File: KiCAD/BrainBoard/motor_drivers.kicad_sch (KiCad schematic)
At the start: 4 parts, among them U2 DRV8231ADSG

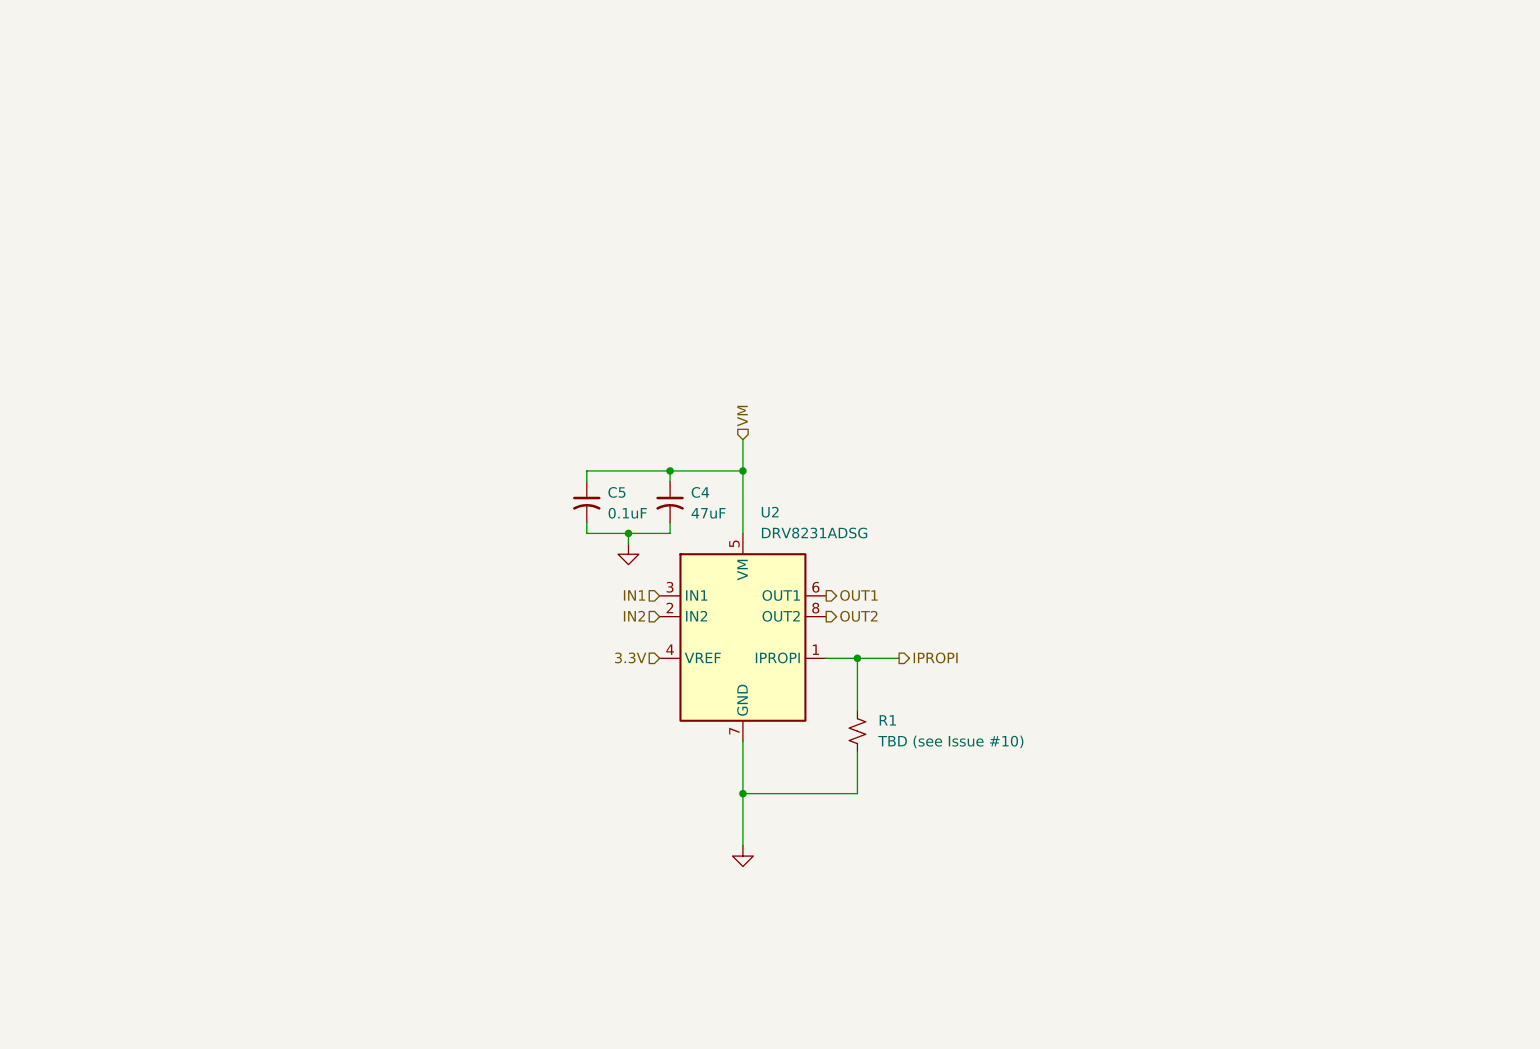
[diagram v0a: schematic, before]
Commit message: [feature] Finalize DRV8231DSGR motor drivers
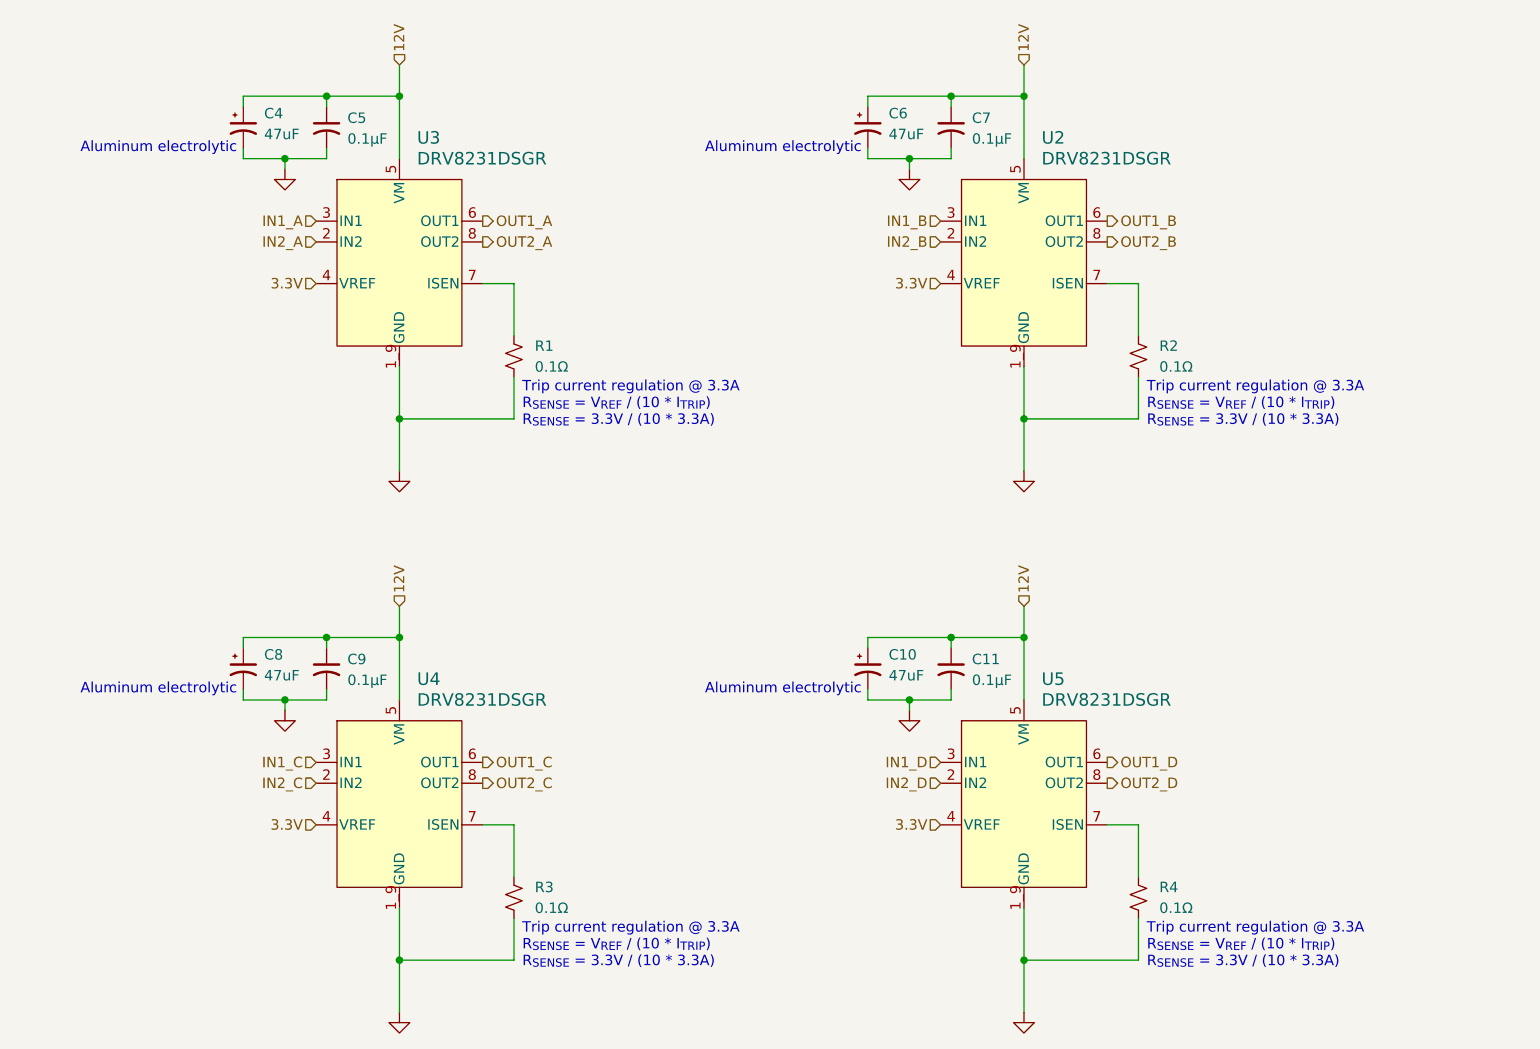
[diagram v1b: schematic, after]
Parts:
- removed C4: 47uF, symbol Device:C_Small_US
- removed U2: DRV8231ADSG, Package_SON:WSON-8-1EP_2x2mm_P0.5mm_EP0.9x1.6mm, symbol Driver_Motor:DRV8231ADSG
- added C10, C4, C6, C8: 47uF, symbol Device:C_Polarized_Small_US
- added C11, C7, C9: 0.1µF, symbol Device:C_Small_US
- added R2, R3, R4: 0.1Ω, symbol Device:R_Small_US
- added U2, U3, U4, U5: DRV8231DSGR, WSON8_DRV8231_TEX, symbol DRV8231DSGR:DRV8231DSGR
- C5: value 0.1uF -> 0.1µF
- R1: value TBD (see Issue #10) -> 0.1Ω
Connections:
- net 3.3V: now also U2.4 (VREF), U3.4 (VREF), U4.4 (VREF), U5.4 (VREF)
- net GND: now also C10.2, C11.2, C4.2, C6.2, C7.2, C8.2, C9.2, R2.2, R3.2, R4.2, U2.1_9 (GND), U3.1_9 (GND), U4.1_9 (GND), U5.1_9 (GND)
- net IPROPI: no longer names the net of R1.1
- net IPROPI: now also U3.7 (ISEN)
- net VM renamed 12V
- net 12V: now also C10.1, C11.1, C4.1, C6.1, C7.1, C8.1, C9.1, U2.5 (VM), U3.5 (VM), U4.5 (VM), U5.5 (VM)
- new net: R3.1, U4.7 (ISEN)
- new net: R2.1, U2.7 (ISEN)
- new net: R4.1, U5.7 (ISEN)
- new net IN1_A: U3.3 (IN1)
- new net IN1_B: U2.3 (IN1)
- new net IN1_C: U4.3 (IN1)
- new net IN1_D: U5.3 (IN1)
- new net IN2_A: U3.2 (IN2)
- new net IN2_B: U2.2 (IN2)
- new net IN2_C: U4.2 (IN2)
- new net IN2_D: U5.2 (IN2)
- new net OUT1_A: U3.6 (OUT1)
- new net OUT1_B: U2.6 (OUT1)
- new net OUT1_C: U4.6 (OUT1)
- new net OUT1_D: U5.6 (OUT1)
- new net OUT2_A: U3.8 (OUT2)
- new net OUT2_B: U2.8 (OUT2)
- new net OUT2_C: U4.8 (OUT2)
- new net OUT2_D: U5.8 (OUT2)
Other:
- note added: "Aluminum electrolytic"
- note added: "Trip current regulation @ 3.3A R_{SENSE} = V_{REF} / (10 * I_{TRIP}) R_{SENSE} = 3.3V / (10 * 3.3A)"
- moved on the sheet: C5, R1

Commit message: fix: Make DRC happy
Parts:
- U2, U3, U4, U5: footprint WSON8_DRV8231_TEX -> footprints:WSON8_DRV8231_TEX
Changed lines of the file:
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@@
 			)
 		)
-		(property "Footprint" "WSON8_DRV8231_TEX"
+		(property "Footprint" "footprints:WSON8_DRV8231_TEX"
 			(at 97.79 50.8 0)
 			(effects
@@
 			)
 		)
-		(property "Footprint" "WSON8_DRV8231_TEX"
+		(property "Footprint" "footprints:WSON8_DRV8231_TEX"
 			(at 173.99 50.8 0)
 			(effects
@@
 			)
 		)
-		(property "Footprint" "WSON8_DRV8231_TEX"
+		(property "Footprint" "footprints:WSON8_DRV8231_TEX"
 			(at 97.79 116.84 0)
 			(effects
@@
 			)
 		)
-		(property "Footprint" "WSON8_DRV8231_TEX"
+		(property "Footprint" "footprints:WSON8_DRV8231_TEX"
 			(at 173.99 116.84 0)
 			(effects

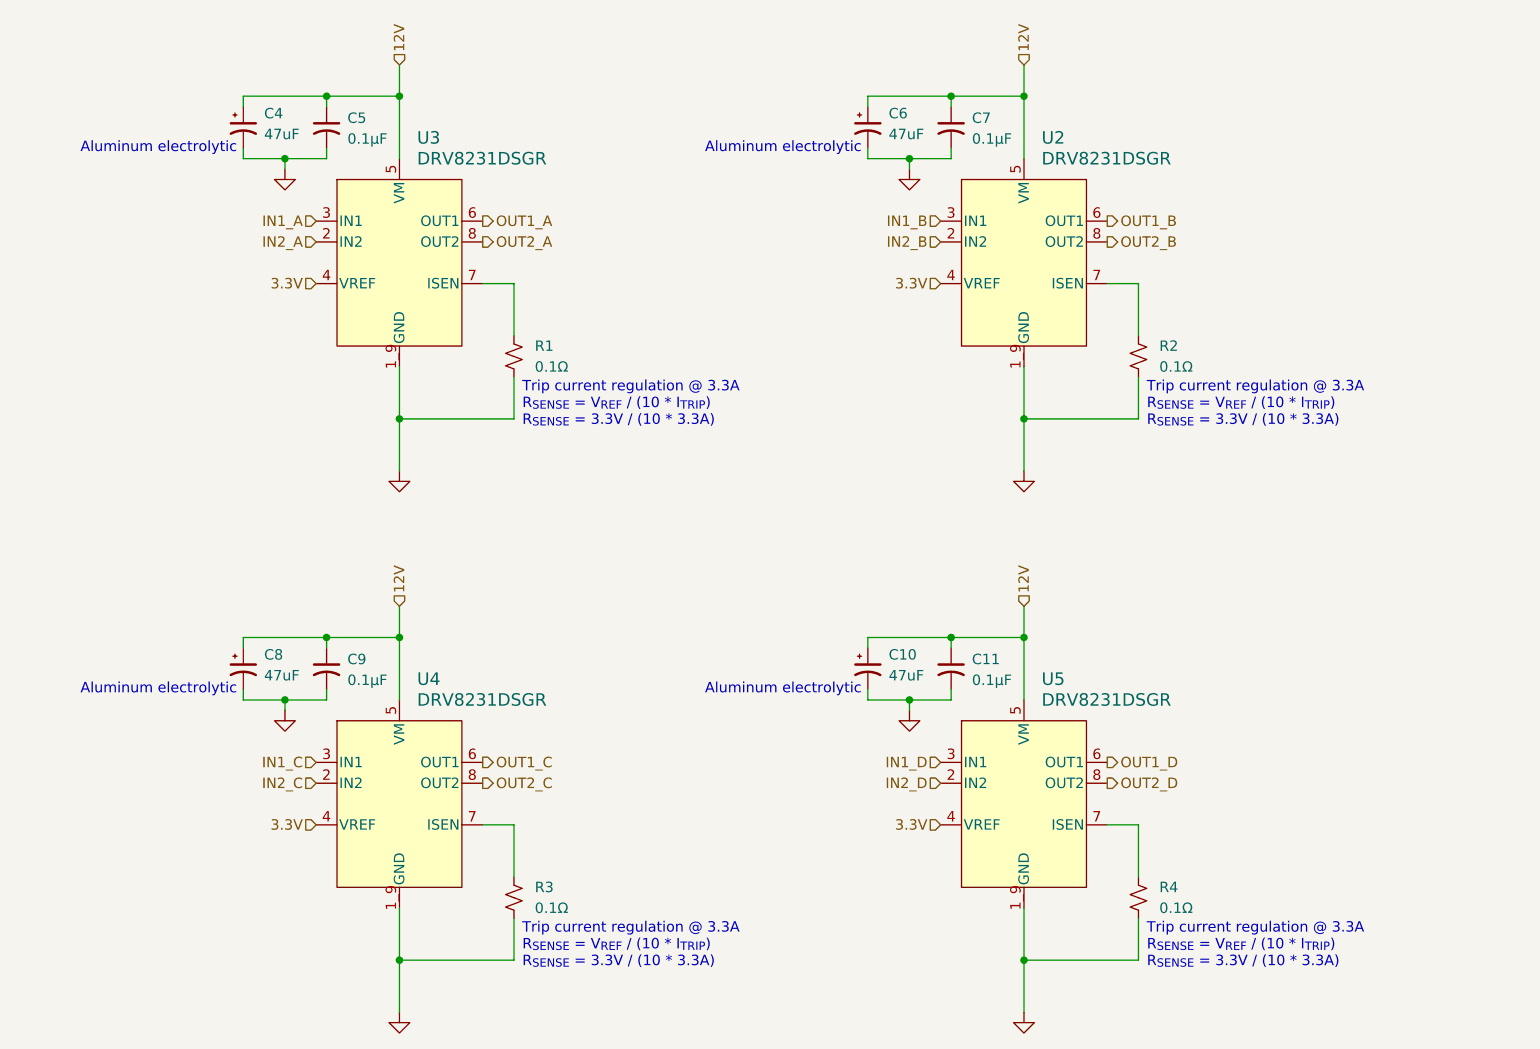
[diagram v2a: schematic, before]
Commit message: feat: battery input
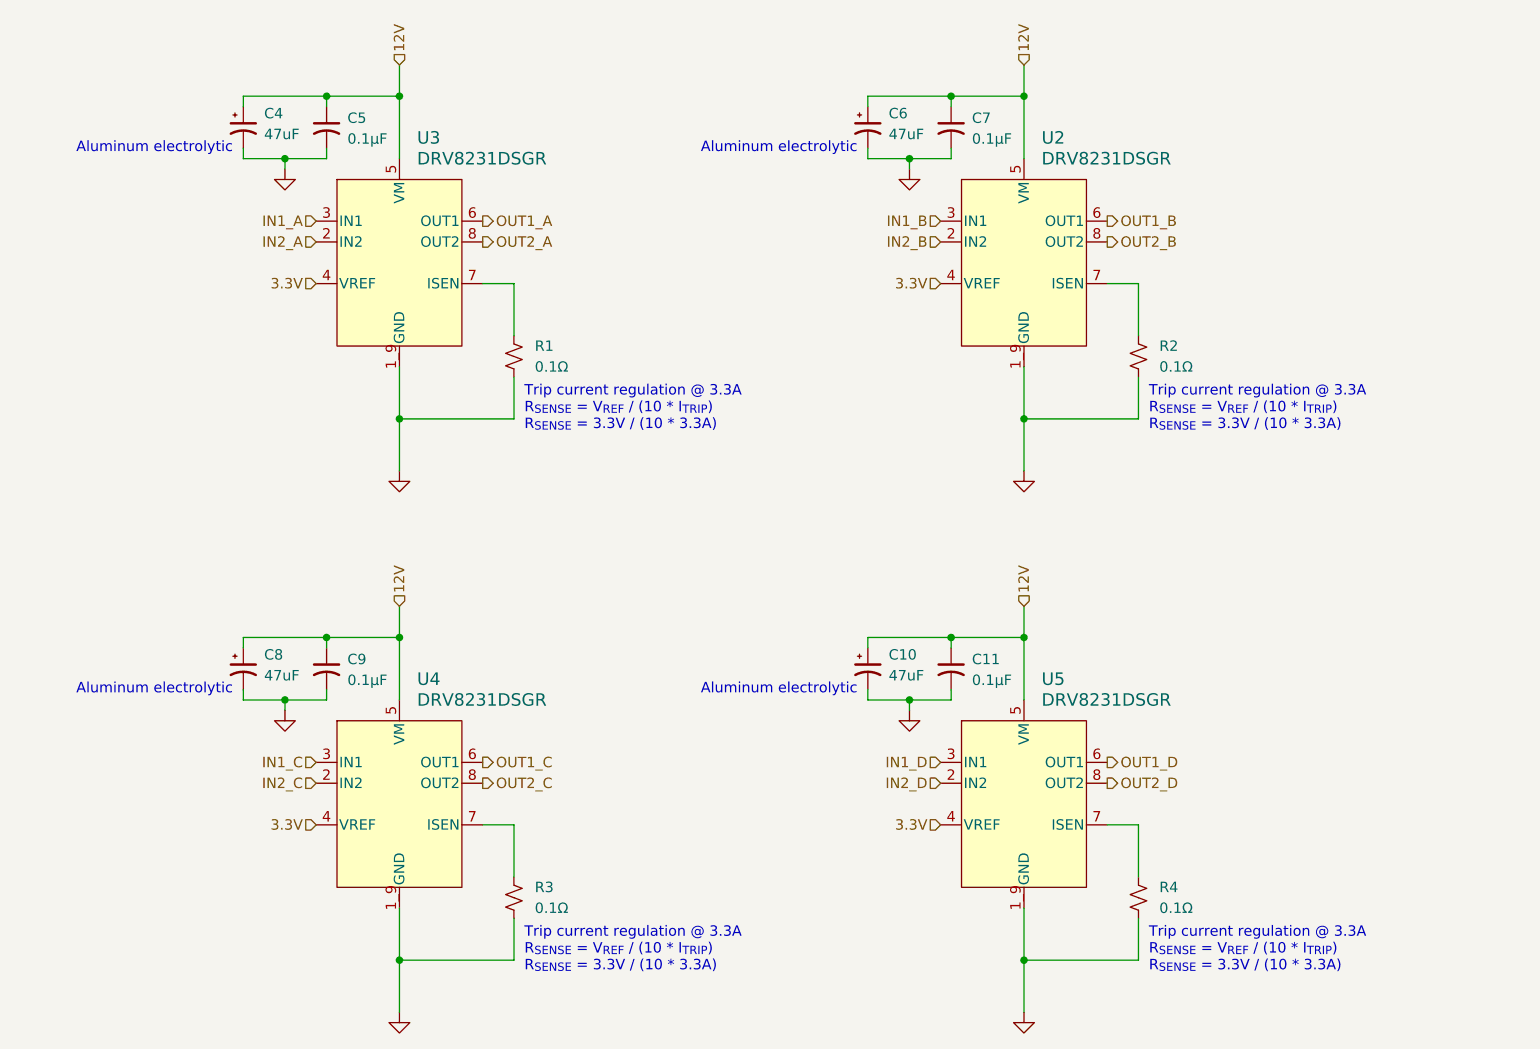
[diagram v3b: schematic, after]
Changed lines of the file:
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@@
 	(text "Trip current regulation @ 3.3A\nR_{SENSE} = V_{REF} / (10 * I_{TRIP})\nR_{SENSE} = 3.3V / (10 * 3.3A)"
 		(exclude_from_sim no)
-		(at 112.776 68.072 0)
+		(at 113.03 68.58 0)
 		(effects
 			(font
@@
 	(text "Trip current regulation @ 3.3A\nR_{SENSE} = V_{REF} / (10 * I_{TRIP})\nR_{SENSE} = 3.3V / (10 * 3.3A)"
 		(exclude_from_sim no)
-		(at 188.976 134.112 0)
+		(at 189.23 134.62 0)
 		(effects
 			(font
@@
 	(text "Aluminum electrolytic"
 		(exclude_from_sim no)
-		(at 77.978 102.87 0)
+		(at 77.47 102.87 0)
 		(effects
 			(font
@@
 	(text "Aluminum electrolytic"
 		(exclude_from_sim no)
-		(at 154.178 36.83 0)
+		(at 153.67 36.83 0)
 		(effects
 			(font
@@
 	(text "Aluminum electrolytic"
 		(exclude_from_sim no)
-		(at 77.978 36.83 0)
+		(at 77.47 36.83 0)
 		(effects
 			(font
@@
 	(text "Trip current regulation @ 3.3A\nR_{SENSE} = V_{REF} / (10 * I_{TRIP})\nR_{SENSE} = 3.3V / (10 * 3.3A)"
 		(exclude_from_sim no)
-		(at 188.976 68.072 0)
+		(at 189.23 68.58 0)
 		(effects
 			(font
@@
 	(text "Trip current regulation @ 3.3A\nR_{SENSE} = V_{REF} / (10 * I_{TRIP})\nR_{SENSE} = 3.3V / (10 * 3.3A)"
 		(exclude_from_sim no)
-		(at 112.776 134.112 0)
+		(at 113.03 134.62 0)
 		(effects
 			(font
@@
 	(text "Aluminum electrolytic"
 		(exclude_from_sim no)
-		(at 154.178 102.87 0)
+		(at 153.67 102.87 0)
 		(effects
 			(font

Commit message: Assigned most general footprints
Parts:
- C11, C5, C7, C9: footprint (none) -> Capacitor_SMD:C_0805_2012Metric
- R1, R2, R3, R4: footprint (none) -> Resistor_SMD:R_0805_2012Metric
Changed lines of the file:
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@@
 			)
 		)
-		(property "Footprint" ""
+		(property "Footprint" "Resistor_SMD:R_0805_2012Metric"
 			(at 111.76 62.23 0)
 			(effects
@@
 			)
 		)
-		(property "Footprint" ""
+		(property "Footprint" "Capacitor_SMD:C_0805_2012Metric"
 			(at 165.1 34.29 0)
 			(effects
@@
 			)
 		)
-		(property "Footprint" ""
+		(property "Footprint" "Resistor_SMD:R_0805_2012Metric"
 			(at 111.76 128.27 0)
 			(effects
@@
 			)
 		)
-		(property "Footprint" ""
+		(property "Footprint" "Capacitor_SMD:C_0805_2012Metric"
 			(at 88.9 100.33 0)
 			(effects
@@
 			)
 		)
-		(property "Footprint" ""
+		(property "Footprint" "Resistor_SMD:R_0805_2012Metric"
 			(at 187.96 62.23 0)
 			(effects
@@
 			)
 		)
-		(property "Footprint" ""
+		(property "Footprint" "Capacitor_SMD:C_0805_2012Metric"
 			(at 88.9 34.29 0)
 			(effects
@@
 			)
 		)
-		(property "Footprint" ""
+		(property "Footprint" "Resistor_SMD:R_0805_2012Metric"
 			(at 187.96 128.27 0)
 			(effects
@@
 			)
 		)
-		(property "Footprint" ""
+		(property "Footprint" "Capacitor_SMD:C_0805_2012Metric"
 			(at 165.1 100.33 0)
 			(effects
